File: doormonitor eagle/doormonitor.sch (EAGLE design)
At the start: 12 parts, among them U1 ATTINY84, Y1 8MHz

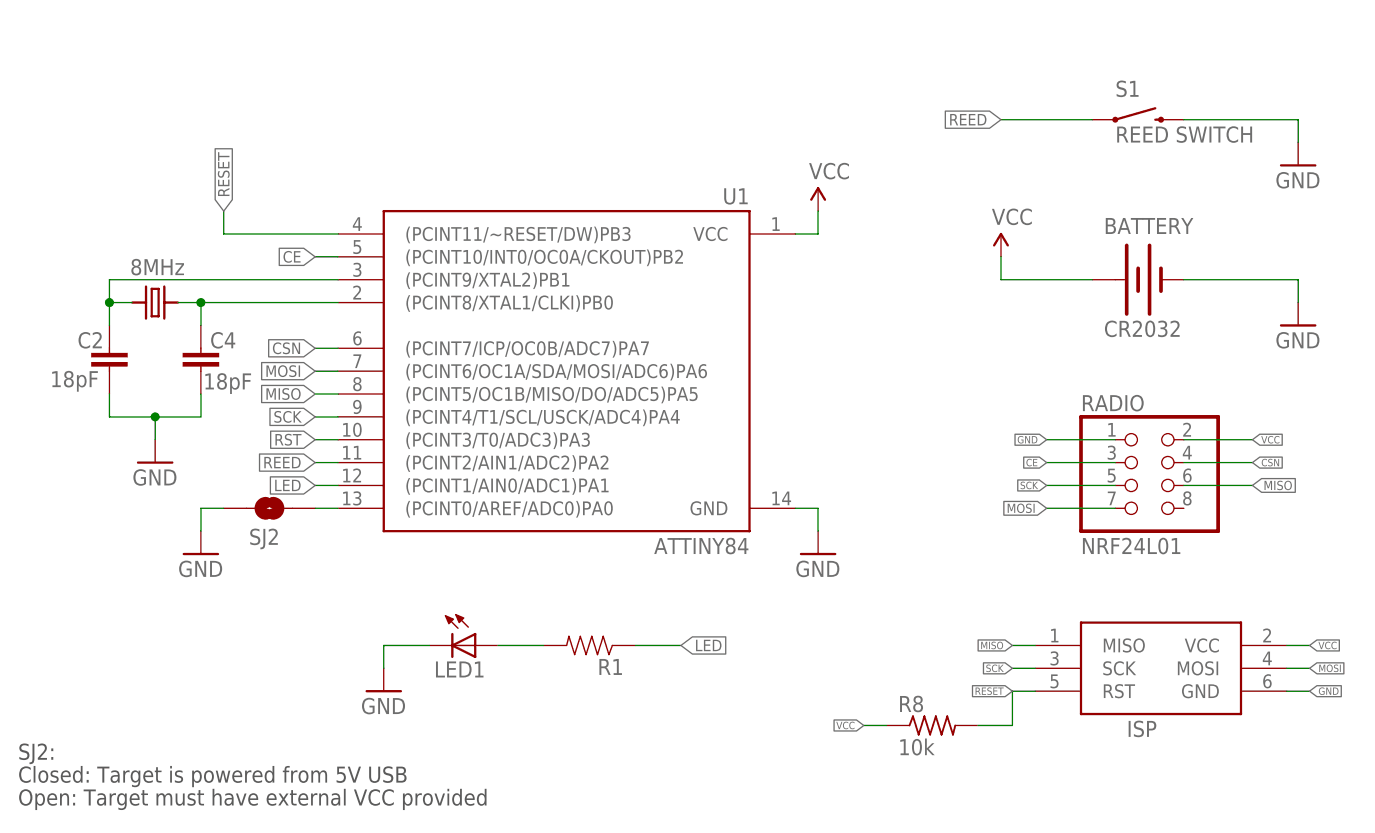
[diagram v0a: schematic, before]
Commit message: Board layout. Includes optional JST connector.
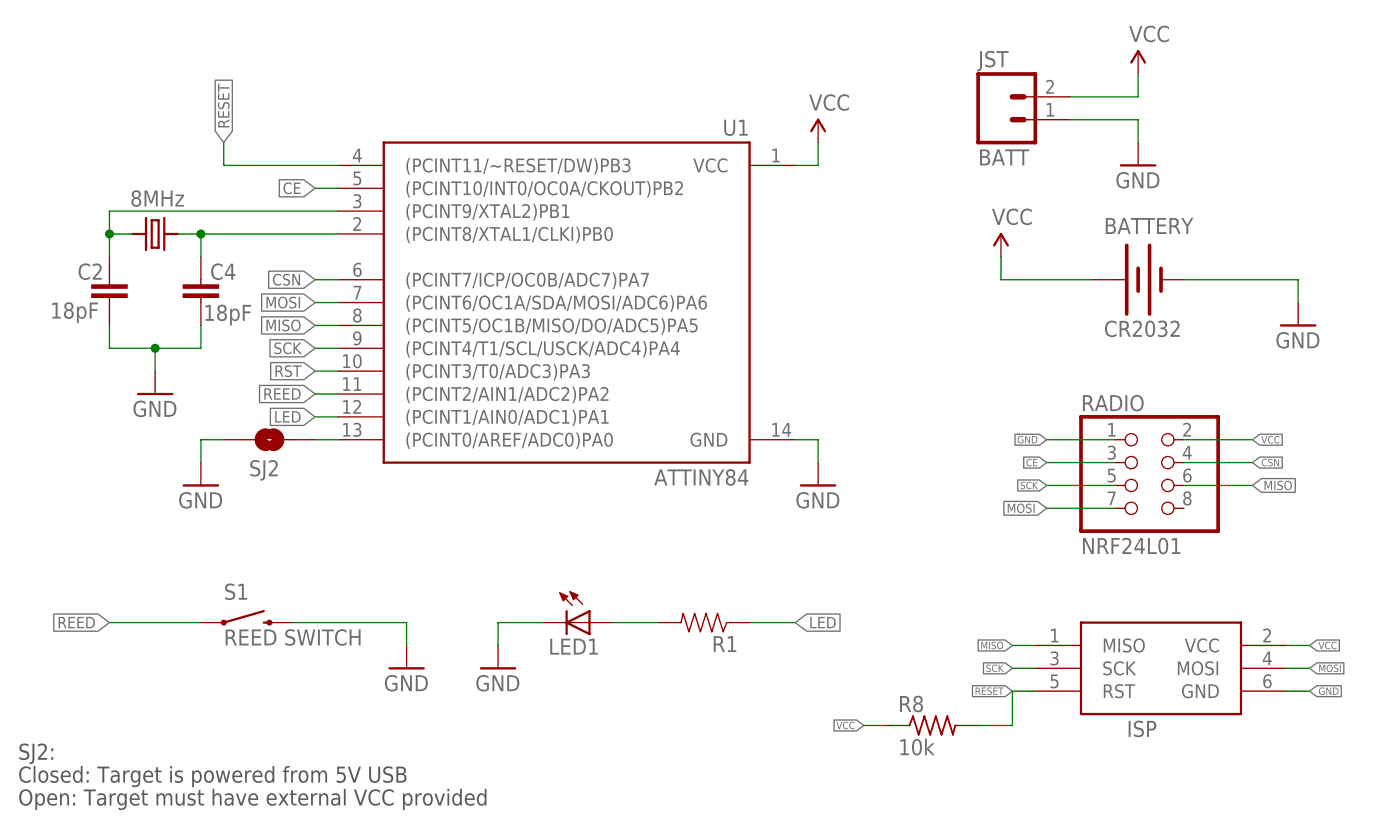
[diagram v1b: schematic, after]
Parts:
- added JST: BATT, SparkFun-Connectors:M02JST-PTH-VERT
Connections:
- net GND: now also JST.1
- net VCC: now also JST.2
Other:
- moved on the sheet: C2, C4, LED1, R1, S1, SJ2, U1

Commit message: Updating schematic.
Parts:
- renumbered SJ2 to SJ1, U1 to MCU
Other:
- note added: "Closed: Receiver"
- note added: "Open: Remote and sensor"
- note added: "SJ1:"
- note removed: "Closed: Target is powered from 5V USB"
- note removed: "Open: Target must have external VCC provided"
- note removed: "SJ2:"
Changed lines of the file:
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@@
 <part name="C2" library="SparkFun-Passives" deviceset="CAP" device="0402-CAP" value="18pF"/>
 <part name="C4" library="SparkFun-Passives" deviceset="CAP" device="0402-CAP" value="18pF"/>
-<part name="SJ2" library="SparkFun-Passives" deviceset="SOLDERJUMPER" device="NC" value="Receiver?"/>
-<part name="U1" library="SparkFun-DigitalIC" deviceset="ATTINY84" device=""/>
+<part name="SJ1" library="SparkFun-Passives" deviceset="SOLDERJUMPER" device="NC" value="Receiver?"/>
+<part name="MCU" library="SparkFun-DigitalIC" deviceset="ATTINY84" device=""/>
 <part name="SUPPLY2" library="SparkFun-Aesthetics" deviceset="VCC" device=""/>
 <part name="GND12" library="SparkFun-Aesthetics" deviceset="GND" device=""/>
@@
 <sheet>
 <plain>
-<text x="2.54" y="5.08" size="1.778" layer="97">Closed: Target is powered from 5V USB</text>
-<text x="2.54" y="2.54" size="1.778" layer="97">Open: Target must have external VCC provided</text>
-<text x="2.54" y="7.62" size="1.778" layer="97">SJ2:</text>
+<text x="2.54" y="5.08" size="1.778" layer="97">Closed: Receiver</text>
+<text x="2.54" y="2.54" size="1.778" layer="97">Open: Remote and sensor</text>
+<text x="2.54" y="7.62" size="1.778" layer="97">SJ1:</text>
 </plain>
 <instances>
@@
 <attribute name="VALUE" x="23.114" y="56.388" size="1.778" layer="96"/>
 </instance>
-<instance part="SJ2" gate="1" x="30.48" y="43.18" smashed="yes">
+<instance part="SJ1" gate="1" x="30.48" y="43.18" smashed="yes">
 <attribute name="NAME" x="28.194" y="39.116" size="1.778" layer="95"/>
 </instance>
-<instance part="U1" gate="G$1" x="63.5" y="58.42" rot="MR0"/>
+<instance part="MCU" gate="G$1" x="63.5" y="58.42" rot="MR0"/>
 <instance part="SUPPLY2" gate="1" x="91.44" y="76.2"/>
 <instance part="GND12" gate="1" x="91.44" y="38.1"/>
@@
 <segment>
 <wire x1="91.44" y1="43.18" x2="91.44" y2="40.64" width="0.1524" layer="91"/>
-<pinref part="U1" gate="G$1" pin="GND"/>
+<pinref part="MCU" gate="G$1" pin="GND"/>
 <wire x1="91.44" y1="43.18" x2="88.9" y2="43.18" width="0.1524" layer="91"/>
 <pinref part="GND12" gate="1" pin="GND"/>
@@
 </segment>
 <segment>
-<pinref part="SJ2" gate="1" pin="1"/>
+<pinref part="SJ1" gate="1" pin="1"/>
 <pinref part="GND1" gate="1" pin="GND"/>
 <wire x1="25.4" y1="43.18" x2="22.86" y2="43.18" width="0.1524" layer="91"/>
@@
 <segment>
 <wire x1="35.56" y1="55.88" x2="38.1" y2="55.88" width="0.1524" layer="91"/>
-<pinref part="U1" gate="G$1" pin="(PCINT5/OC1B/MISO/DO/ADC5)PA5"/>
+<pinref part="MCU" gate="G$1" pin="(PCINT5/OC1B/MISO/DO/ADC5)PA5"/>
 <label x="35.56" y="55.88" size="1.27" layer="95" rot="MR0" xref="yes"/>
 </segment>
@@
 <segment>
 <wire x1="35.56" y1="58.42" x2="38.1" y2="58.42" width="0.1524" layer="91"/>
-<pinref part="U1" gate="G$1" pin="(PCINT6/OC1A/SDA/MOSI/ADC6)PA6"/>
+<pinref part="MCU" gate="G$1" pin="(PCINT6/OC1A/SDA/MOSI/ADC6)PA6"/>
 <label x="35.56" y="58.42" size="1.27" layer="95" rot="MR0" xref="yes"/>
 </segment>
@@
 <segment>
 <wire x1="35.56" y1="53.34" x2="38.1" y2="53.34" width="0.1524" layer="91"/>
-<pinref part="U1" gate="G$1" pin="(PCINT4/T1/SCL/USCK/ADC4)PA4"/>
+<pinref part="MCU" gate="G$1" pin="(PCINT4/T1/SCL/USCK/ADC4)PA4"/>
 <label x="35.56" y="53.34" size="1.27" layer="95" rot="MR0" xref="yes"/>
 </segment>
@@
 <segment>
 <wire x1="91.44" y1="73.66" x2="91.44" y2="76.2" width="0.1524" layer="91"/>
-<pinref part="U1" gate="G$1" pin="VCC"/>
+<pinref part="MCU" gate="G$1" pin="VCC"/>
 <wire x1="88.9" y1="73.66" x2="91.44" y2="73.66" width="0.1524" layer="91"/>
 <pinref part="SUPPLY2" gate="1" pin="VCC"/>
@@
 <segment>
 <label x="25.4" y="76.2" size="1.27" layer="95" rot="MR90" xref="yes"/>
-<pinref part="U1" gate="G$1" pin="(PCINT11/~RESET/DW)PB3"/>
+<pinref part="MCU" gate="G$1" pin="(PCINT11/~RESET/DW)PB3"/>
 <wire x1="25.4" y1="73.66" x2="38.1" y2="73.66" width="0.1524" layer="91"/>
 <wire x1="25.4" y1="76.2" x2="25.4" y2="73.66" width="0.1524" layer="91"/>
@@
 <segment>
 <wire x1="38.1" y1="71.12" x2="35.56" y2="71.12" width="0.1524" layer="91"/>
-<pinref part="U1" gate="G$1" pin="(PCINT10/INT0/OC0A/CKOUT)PB2"/>
+<pinref part="MCU" gate="G$1" pin="(PCINT10/INT0/OC0A/CKOUT)PB2"/>
 <label x="35.56" y="71.12" size="1.27" layer="95" rot="MR0" xref="yes"/>
 </segment>
@@
 <segment>
 <wire x1="38.1" y1="60.96" x2="35.56" y2="60.96" width="0.1524" layer="91"/>
-<pinref part="U1" gate="G$1" pin="(PCINT7/ICP/OC0B/ADC7)PA7"/>
+<pinref part="MCU" gate="G$1" pin="(PCINT7/ICP/OC0B/ADC7)PA7"/>
 <label x="35.56" y="60.96" size="1.27" layer="95" rot="MR0" xref="yes"/>
 </segment>
@@
 <segment>
 <wire x1="35.56" y1="50.8" x2="38.1" y2="50.8" width="0.1524" layer="91"/>
-<pinref part="U1" gate="G$1" pin="(PCINT3/T0/ADC3)PA3"/>
+<pinref part="MCU" gate="G$1" pin="(PCINT3/T0/ADC3)PA3"/>
 <label x="35.56" y="50.8" size="1.27" layer="95" rot="MR0" xref="yes"/>
 </segment>
@@
 <net name="N$3" class="0">
 <segment>
-<pinref part="U1" gate="G$1" pin="(PCINT9/XTAL2)PB1"/>
+<pinref part="MCU" gate="G$1" pin="(PCINT9/XTAL2)PB1"/>
 <wire x1="38.1" y1="68.58" x2="12.7" y2="68.58" width="0.1524" layer="91"/>
 <pinref part="C2" gate="G$1" pin="1"/>
@@
 <net name="N$4" class="0">
 <segment>
-<pinref part="U1" gate="G$1" pin="(PCINT8/XTAL1/CLKI)PB0"/>
+<pinref part="MCU" gate="G$1" pin="(PCINT8/XTAL1/CLKI)PB0"/>
 <wire x1="38.1" y1="66.04" x2="22.86" y2="66.04" width="0.1524" layer="91"/>
 <pinref part="C4" gate="G$1" pin="1"/>
@@
 <net name="N$2" class="0">
 <segment>
-<pinref part="U1" gate="G$1" pin="(PCINT0/AREF/ADC0)PA0"/>
-<pinref part="SJ2" gate="1" pin="2"/>
+<pinref part="MCU" gate="G$1" pin="(PCINT0/AREF/ADC0)PA0"/>
+<pinref part="SJ1" gate="1" pin="2"/>
 <wire x1="38.1" y1="43.18" x2="35.56" y2="43.18" width="0.1524" layer="91"/>
 </segment>
@@
 <net name="REED" class="0">
 <segment>
-<pinref part="U1" gate="G$1" pin="(PCINT2/AIN1/ADC2)PA2"/>
+<pinref part="MCU" gate="G$1" pin="(PCINT2/AIN1/ADC2)PA2"/>
 <wire x1="38.1" y1="48.26" x2="35.56" y2="48.26" width="0.1524" layer="91"/>
 <label x="35.56" y="48.26" size="1.27" layer="95" rot="R180" xref="yes"/>
@@
 <net name="LED" class="0">
 <segment>
-<pinref part="U1" gate="G$1" pin="(PCINT1/AIN0/ADC1)PA1"/>
+<pinref part="MCU" gate="G$1" pin="(PCINT1/AIN0/ADC1)PA1"/>
 <wire x1="38.1" y1="45.72" x2="35.56" y2="45.72" width="0.1524" layer="91"/>
 <label x="35.56" y="45.72" size="1.27" layer="95" rot="R180" xref="yes"/>

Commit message: Removing unused line.
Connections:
- removed net RST: MCU.(PCINT3/T0/ADC3)PA3
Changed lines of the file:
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@@
-</segment>
-</net>
-<net name="RST" class="0">
-<segment>
-<wire x1="35.56" y1="50.8" x2="38.1" y2="50.8" width="0.1524" layer="91"/>
-<pinref part="MCU" gate="G$1" pin="(PCINT3/T0/ADC3)PA3"/>
-<label x="35.56" y="50.8" size="1.27" layer="95" rot="MR0" xref="yes"/>
 </segment>
 </net>

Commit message: Fixing pinchange.
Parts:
- removed MCU: ATTINY84, SparkFun-DigitalIC:ATTINY84
- added ATTINY84: ATTINY84-20SSU, Atmel_By_element14_Batch_1:ATTINY84-20SSU
- added U$1: VIA, thinkmaketest:VIA
- C2, C4: device SparkFun-Passives:CAP0402-CAP -> SparkFun-Passives:CAP0805
- LED1: device SparkFun-LED:LED10MM -> led:LED5MM
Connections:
- net CE: now also ATTINY84.PA7; no longer MCU.(PCINT10/INT0/OC0A/CKOUT)PB2
- net CSN: now also ATTINY84.PA3; no longer MCU.(PCINT7/ICP/OC0B/ADC7)PA7
- net GND: now also ATTINY84.GND; no longer MCU.GND
- net LED: now also ATTINY84.PA1; no longer MCU.(PCINT1/AIN0/ADC1)PA1
- net MISO: now also ATTINY84.PA5; no longer MCU.(PCINT5/OC1B/MISO/DO/ADC5)PA5
- net MOSI: now also ATTINY84.PA6; no longer MCU.(PCINT6/OC1A/SDA/MOSI/ADC6)PA6
- net N$2: now also ATTINY84.PA0; no longer MCU.(PCINT0/AREF/ADC0)PA0
- net N$3: now also ATTINY84.PB0, U$1.1; no longer MCU.(PCINT9/XTAL2)PB1
- net N$4: now also ATTINY84.PB1; no longer MCU.(PCINT8/XTAL1/CLKI)PB0
- net REED: now also ATTINY84.PA2; no longer MCU.(PCINT2/AIN1/ADC2)PA2
- net RESET: now also ATTINY84.PB3; no longer MCU.(PCINT11/~RESET/DW)PB3
- net SCK: now also ATTINY84.PA4; no longer MCU.(PCINT4/T1/SCL/USCK/ADC4)PA4
- net VCC: now also ATTINY84.VCC; no longer MCU.VCC
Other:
- note added: "Open: Door sensor"
- note removed: "Open: Remote and sensor"
- moved on the sheet: LED1, R1, S1, SJ1
